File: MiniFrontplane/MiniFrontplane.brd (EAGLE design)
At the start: 95.7 x 39.4 mm, 17 parts, among them IC2 74ACT14N, U1 MCP130SOT

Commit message: Frontplane THAT MIGHT WORK THIS TIME
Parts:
- removed C1: 4.7uF, SparkFun-Passives:CAP-PTH-SMALLEZ
- removed IC2: 74ACT14N, 74xx-eu:DIL14
- removed R2: 4k7, SparkFun-Resistors:AXIAL-0.3
- removed R3, R4: 27k, SparkFun-Resistors:AXIAL-0.3
- removed U$1: MINITOGGLE, Benchoff:MINITOGGLE
- removed U$2: MINITACT, Benchoff:MINITACT
- removed U$22, U$4, U$5, U$9: (no value), SparkFun-Electromechanical:STAND-OFF
- added S1: TP11SWITCH, Benchoff:TP11
- added S2: MINITOGGLE, Benchoff:MINITOGGLE
- JP3: value Samtec SLW-103-01-T-S -> (none)
- LED1: device SparkFun-LED:LED5MM -> led:LED5MM
- R1: value 150 -> 220; device SparkFun-Resistors:AXIAL-0.3 -> SparkFun-Resistors:AXIAL-0.3-KIT
- U1: value MCP130SOT -> DS1813; device SparkFun-DigitalIC:SOT23-3 -> Benchoff:TO-92
- moved U1 54.7 mm to (91.6, 22.1), turned to 270 degrees
- moved JP1 26.5 mm to (71.1, 31.8)
- moved JP2 26.5 mm to (30.5, 31.8), turned to 180 degrees
- moved LED1 20.2 mm to (31.4, 21.9), turned to 90 degrees
- moved R1 10.00 mm to (31.8, 15.2), turned to 0 degrees
- moved JP3 8.74 mm to (17.8, 22.9), flipped to the top, turned to 270 degrees
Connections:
- net N$2 renamed PS_OK
- removed net 5VSB: JP1.3
- removed net N$1 (its old number): JP3.1, U$1.P2
- removed net N$4: R3.P$2, R4.P$1, U$2.CON2
- removed net N$5: C1.2, R2.P$2, R3.P$1
- removed net N$6: IC2.13, R2.P$1
- new net PS_ON: JP3.3, S2.L2
- net GND: now also JP2.31, JP3.1, S1.P$2, S2.COM; no longer IC2.7, JP2.2, JP3.3, R4.P$2, U$1.COM
- net RESET: now also JP1.27, S1.P$1; no longer IC2.12, JP2.28
- net VCC: no longer C1.1, IC2.14, U$2.CON1
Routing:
- net GND: track 104.4 -> 38.1 mm
- net N$4: track 45.9 -> 0.00 mm
- net PS_ON: track 0.00 -> 24.4 mm
- net RESET: track 22.7 -> 41.7 mm
- net N$1 (its old number): track 15.8 -> 0.00 mm
- net VCC: track 14.5 -> 0.00 mm
- net N$1: track 16.7 -> 7.14 mm
- net N$5: track 8.70 -> 0.00 mm
- net N$6: track 5.08 -> 0.00 mm
- net PS_OK: track 13.2 -> 12.3 mm
- added copper zone on layer 16, net GND
- added copper zone on layer 1, net VCC
- removed copper zone on layer 1, net GND
- removed copper zone on layer 16, net VCC
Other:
- board size 95.7 x 39.4 mm -> 94.6 x 34.9 mm
- board text added: "*"
- board text added: "5V"
- board text added: "64 Pin Terminal Samtek TLW-132-06-F-D SLW-132-01-F-D"
- board text added: "GND"
- board text removed: "1"
- board text removed: "32"
- board text removed: "4.7uF"
- board text removed: "74LS14"
- board text removed: "A"
- board text removed: "C"
- board text removed: "C&K 7101MDZQE"
- board text removed: "C&K TP11SHZ"
- board text removed: "MCP130"
- board text removed: "Power"
- board text removed: "Reset"

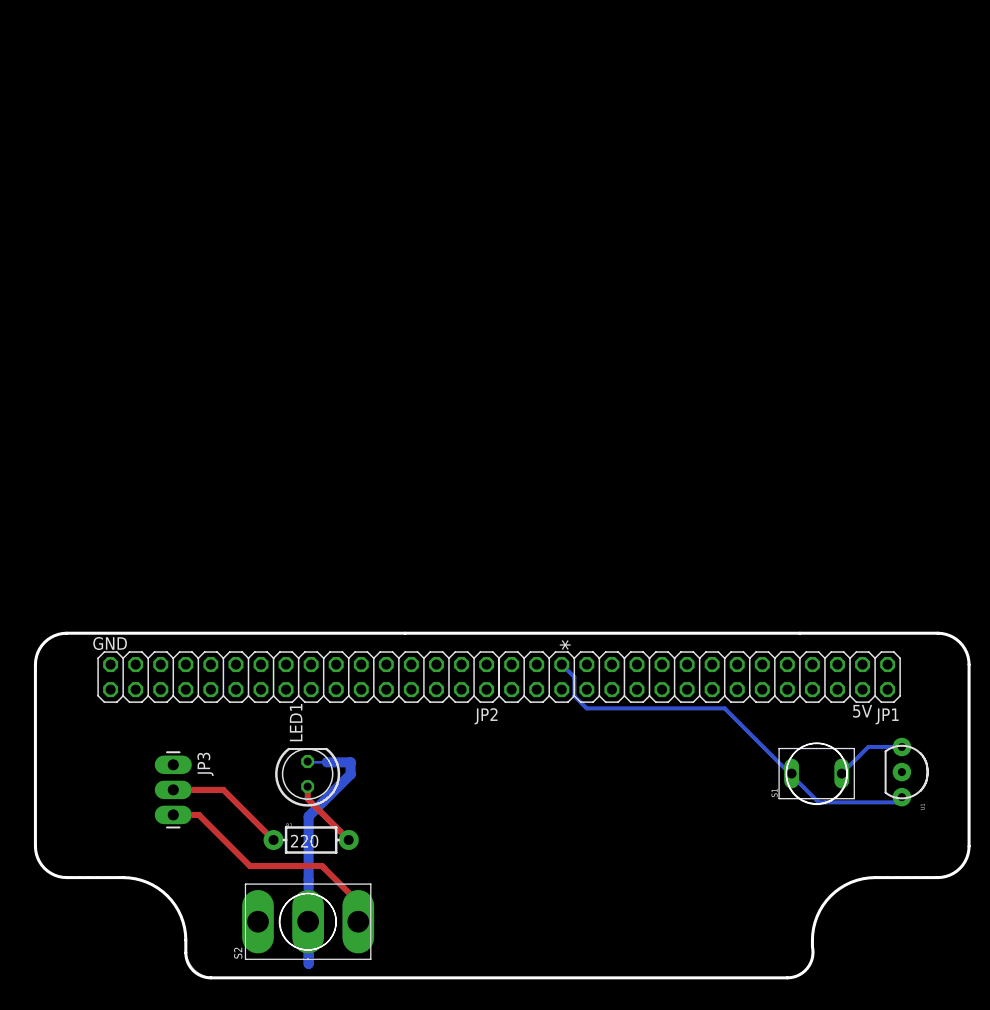
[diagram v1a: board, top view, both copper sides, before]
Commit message: Moved everything 0.03 inches
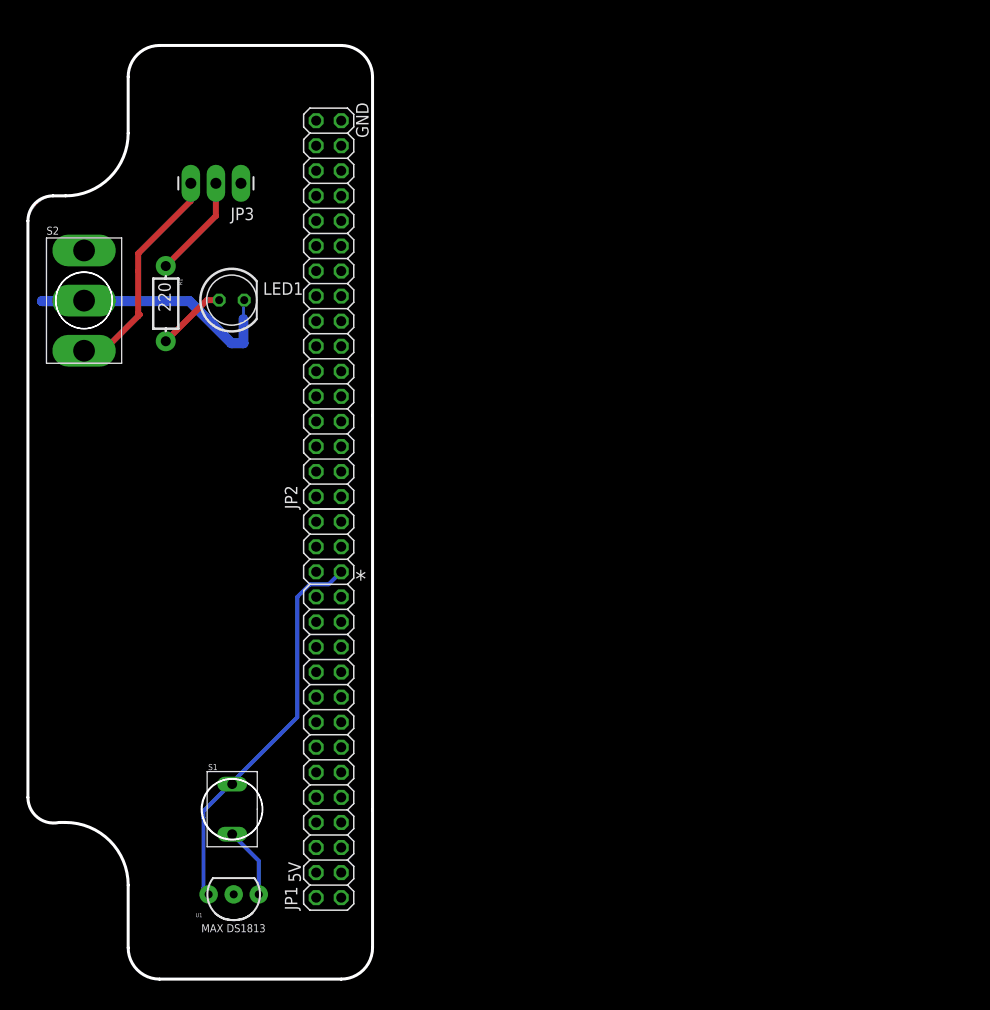
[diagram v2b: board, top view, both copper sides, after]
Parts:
- moved U1 68.8 mm to (23.9, 9.73), turned to 180 degrees
- moved S2 66.9 mm to (8.74, 69.9), turned to 0 degrees
- moved S1 59.3 mm to (23.7, 18.4), turned to 0 degrees
- moved JP3 59.3 mm to (24.6, 81.8), turned to 180 degrees
- moved R1 56.3 mm to (17.0, 69.6), turned to 270 degrees
- moved LED1 48.6 mm to (23.7, 70.0), turned to 0 degrees
- moved JP1 37.7 mm to (33.5, 28.4), turned to 90 degrees
- moved JP2 37.5 mm to (33.5, 69.1), turned to 90 degrees
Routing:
- net PS_OK: track 12.3 -> 10.5 mm
- net RESET: track 41.7 -> 39.9 mm
- net PS_ON: track 24.4 -> 22.7 mm
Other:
- board size 94.6 x 34.9 mm -> 34.9 x 94.6 mm
- board text added: "MAX DS1813"
- board text removed: "64 Pin Terminal Samtek TLW-132-06-F-D SLW-132-01-F-D"

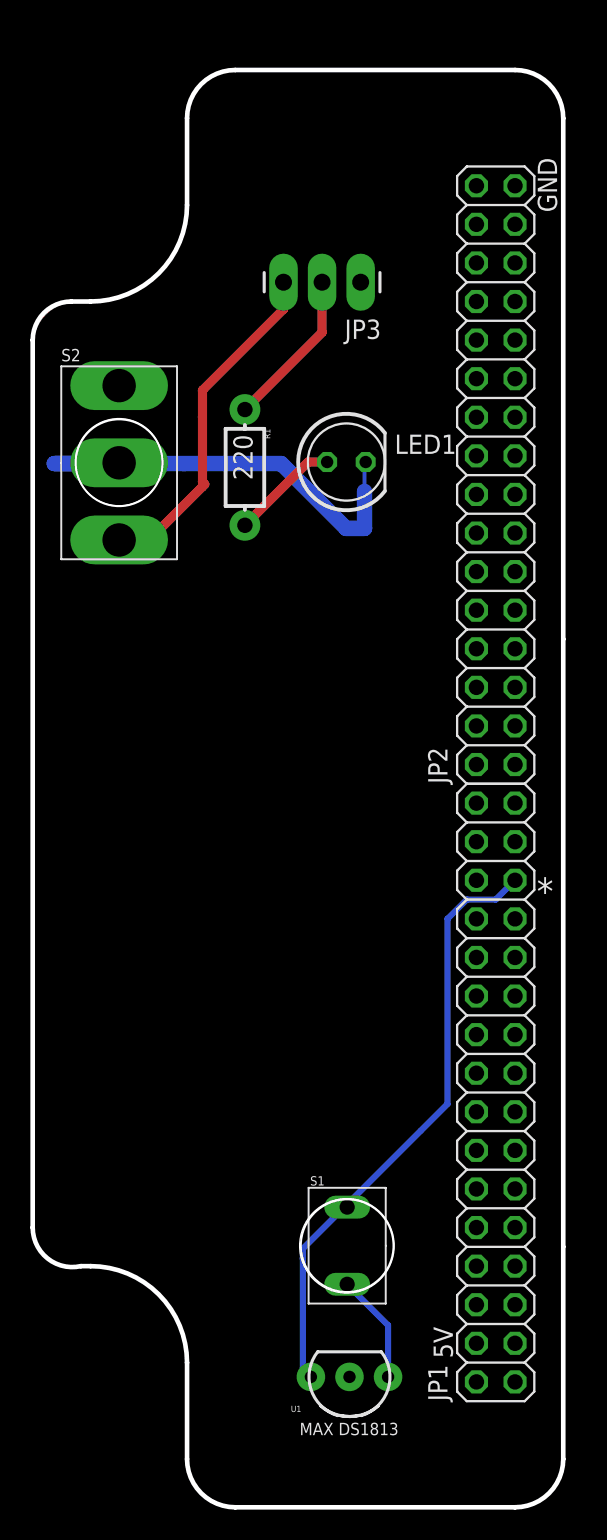
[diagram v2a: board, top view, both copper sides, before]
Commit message: Fixed the mini front plane
It didn't work before, so there ya go
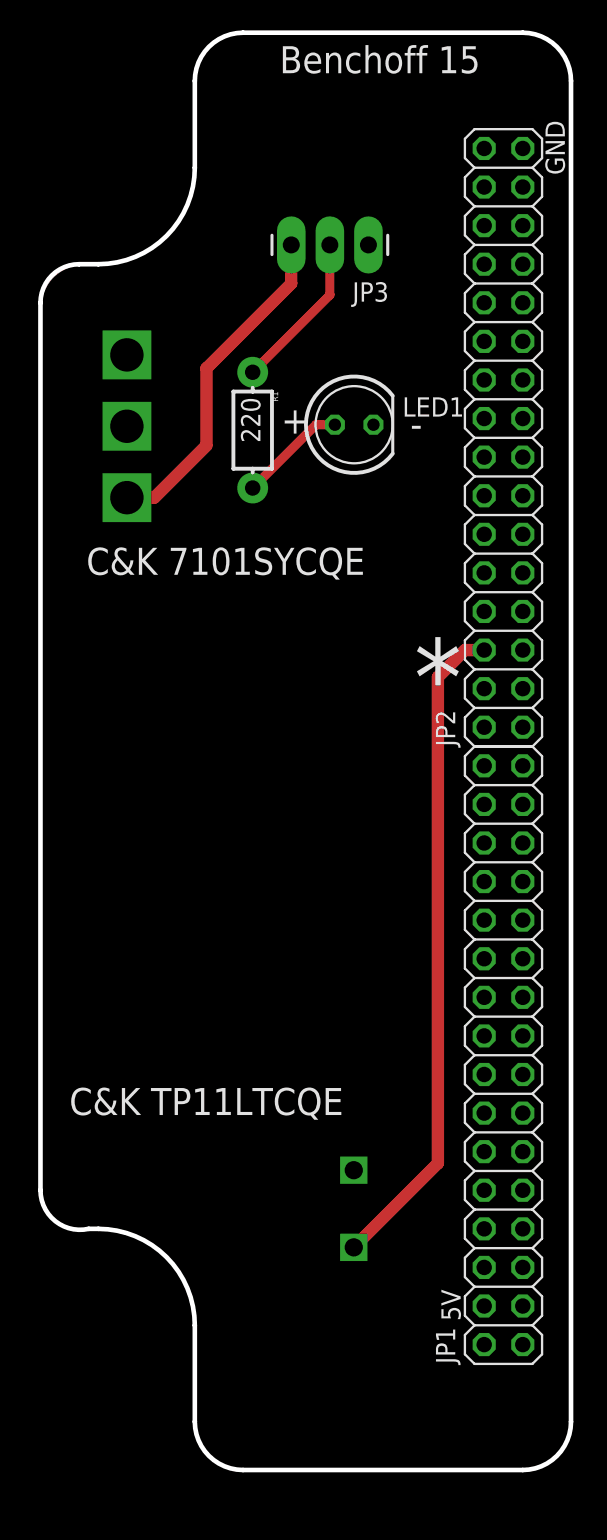
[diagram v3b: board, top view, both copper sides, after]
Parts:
- removed S1: TP11SWITCH, Benchoff:TP11
- removed S2: MINITOGGLE, Benchoff:MINITOGGLE
- removed U1: DS1813, Benchoff:TO-92
- added U$1: 7101, C&K:7101SYCQE
- added U$2: TP11, C&K:TP11
- moved JP2 2.51 mm to (34.0, 71.5)
- moved JP3 2.51 mm to (25.1, 84.2)
- moved LED1 2.51 mm to (24.2, 72.4)
- moved JP1 2.51 mm to (34.0, 30.9)
- moved R1 2.51 mm to (17.5, 72.1)
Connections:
- net GND: now also U$1.COMM, U$2.1; no longer S1.P$2, S2.COM, U1.3
- net PS_ON: now also U$1.3; no longer S2.L2
- net RESET: now also JP2.6, U$2.2; no longer JP1.27, S1.P$1, U1.1
- net VCC: no longer U1.2
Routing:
- net GND: track 38.1 -> 0.00 mm
- net RESET: track 39.9 -> 43.6 mm
- net PS_ON: track 22.7 -> 22.2 mm
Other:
- outline, holes or cut-outs redrawn
- board text added: "+"
- board text added: "-"
- board text added: "Benchoff 15"
- board text added: "C&K 7101SYCQE"
- board text added: "C&K TP11LTCQE"
- board text removed: "MAX DS1813"
